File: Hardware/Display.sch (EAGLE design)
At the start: 54 parts, among them IC1 STM32F030C6T, IC2 VREG-TS1117CW-3V3, M1 WIRELESS-NRF24L01, Q1 BSS138, Q10 BSS138, Q11 IRLML5203, Q12 BSS138, Q13 IRLML5203, Q14 BSS138, Q15 IRLML5203, Q16 BSS138, Q2 BSS138, Q3 BSS138, Q4 BSS138, Q5 BSS138, Q6 BSS138, Q7 BSS138, Q8 BSS138, Q9 IRLML5203

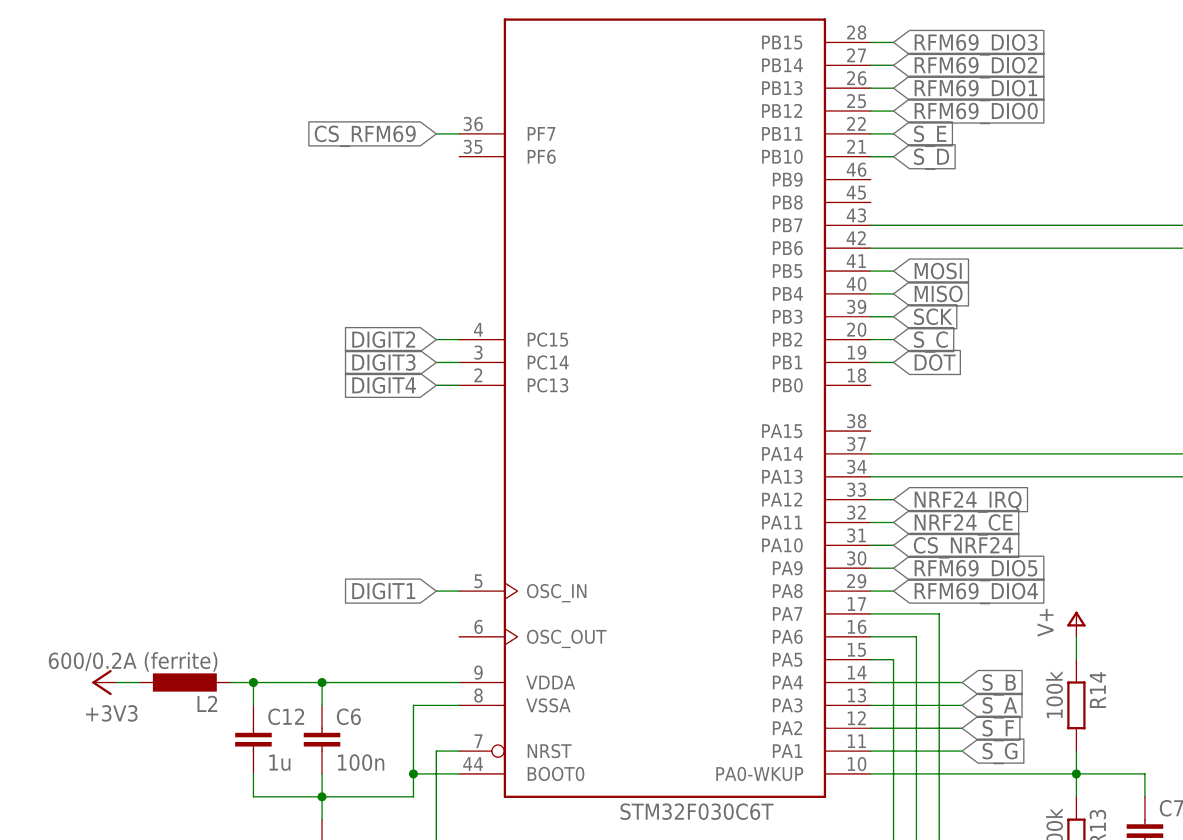
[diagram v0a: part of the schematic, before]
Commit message: Added crystal to display board
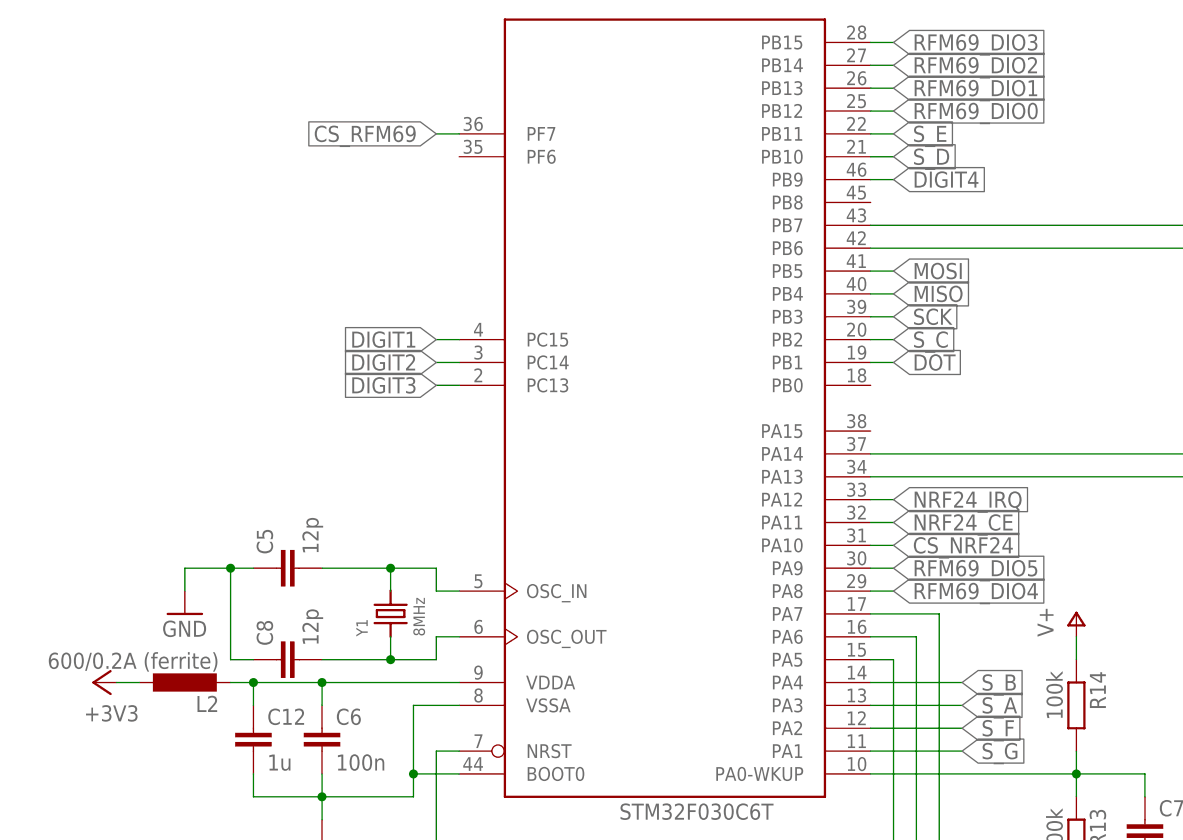
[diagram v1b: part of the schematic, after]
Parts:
- added C5, C8: 12p, rcl:C-EUC0603
- added Y1: 8MHz, abracon:CRYSTAL.3.2X2.5MM
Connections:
- new net N$15: C5.2, IC1MCU.OSC_IN, Y1.2
- new net N$19: C8.2, IC1MCU.OSC_OUT, Y1.1
- net DIGIT1: now also IC1MCU.PC15; no longer IC1MCU.OSC_IN
- net DIGIT2: now also IC1MCU.PC14; no longer IC1MCU.PC15
- net DIGIT3: now also IC1MCU.PC13; no longer IC1MCU.PC14
- net DIGIT4: now also IC1MCU.PB9; no longer IC1MCU.PC13
- net GND: now also C5.1, C8.1
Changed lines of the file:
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@@
 <part name="IN2" library="con-lstb" deviceset="MA07-1" device=""/>
 <part name="OUT2" library="con-lstb" deviceset="MA07-1" device=""/>
+<part name="Y1" library="abracon" deviceset="CRYSTAL" device=".3.2X2.5MM" value="8MHz"/>
+<part name="C5" library="rcl" deviceset="C-EU" device="C0603" value="12p"/>
+<part name="C8" library="rcl" deviceset="C-EU" device="C0603" value="12p"/>
+<part name="GND22" library="supply1" deviceset="GND" device=""/>
 </parts>
 <sheets>
@@
 <instance part="IN2" gate="1" x="533.4" y="5.08" rot="R90"/>
 <instance part="OUT2" gate="1" x="533.4" y="60.96" rot="MR270"/>
+<instance part="Y1" gate="G$1" x="127" y="-15.24" rot="R90"/>
+<instance part="C5" gate="G$1" x="114.3" y="-10.16" rot="R90"/>
+<instance part="C8" gate="G$1" x="114.3" y="-20.32" rot="R90"/>
+<instance part="GND22" gate="1" x="104.14" y="-15.24"/>
 </instances>
 <busses>
@@
 <wire x1="223.52" y1="25.4" x2="223.52" y2="15.24" width="0.1524" layer="91"/>
 </segment>
+<segment>
+<pinref part="GND22" gate="1" pin="GND"/>
+<wire x1="104.14" y1="-12.7" x2="104.14" y2="-10.16" width="0.1524" layer="91"/>
+<pinref part="C5" gate="G$1" pin="1"/>
+<wire x1="104.14" y1="-10.16" x2="109.22" y2="-10.16" width="0.1524" layer="91"/>
+<pinref part="C8" gate="G$1" pin="1"/>
+<wire x1="109.22" y1="-10.16" x2="111.76" y2="-10.16" width="0.1524" layer="91"/>
+<wire x1="111.76" y1="-20.32" x2="109.22" y2="-20.32" width="0.1524" layer="91"/>
+<wire x1="109.22" y1="-20.32" x2="109.22" y2="-10.16" width="0.1524" layer="91"/>
+<junction x="109.22" y="-10.16"/>
+</segment>
 </net>
 <net name="SCK" class="0">
@@
 </segment>
 <segment>
-<pinref part="IC1" gate="MCU" pin="OSC_IN"/>
-<wire x1="134.62" y1="-12.7" x2="132.08" y2="-12.7" width="0.1524" layer="91"/>
-<label x="132.08" y="-12.7" size="1.778" layer="95" rot="R180" xref="yes"/>
+<pinref part="IC1" gate="MCU" pin="PC15"/>
+<wire x1="134.62" y1="15.24" x2="132.08" y2="15.24" width="0.1524" layer="91"/>
+<label x="132.08" y="15.24" size="1.778" layer="95" rot="R180" xref="yes"/>
 </segment>
 </net>
@@
 </segment>
 <segment>
-<pinref part="IC1" gate="MCU" pin="PC15"/>
-<wire x1="134.62" y1="15.24" x2="132.08" y2="15.24" width="0.1524" layer="91"/>
-<label x="132.08" y="15.24" size="1.778" layer="95" rot="R180" xref="yes"/>
+<pinref part="IC1" gate="MCU" pin="PC14"/>
+<wire x1="134.62" y1="12.7" x2="132.08" y2="12.7" width="0.1524" layer="91"/>
+<label x="132.08" y="12.7" size="1.778" layer="95" rot="R180" xref="yes"/>
 </segment>
 </net>
@@
 </segment>
 <segment>
-<pinref part="IC1" gate="MCU" pin="PC14"/>
-<wire x1="134.62" y1="12.7" x2="132.08" y2="12.7" width="0.1524" layer="91"/>
-<label x="132.08" y="12.7" size="1.778" layer="95" rot="R180" xref="yes"/>
+<pinref part="IC1" gate="MCU" pin="PC13"/>
+<wire x1="134.62" y1="10.16" x2="132.08" y2="10.16" width="0.1524" layer="91"/>
+<label x="132.08" y="10.16" size="1.778" layer="95" rot="R180" xref="yes"/>
 </segment>
 </net>
@@
 </segment>
 <segment>
-<pinref part="IC1" gate="MCU" pin="PC13"/>
-<wire x1="134.62" y1="10.16" x2="132.08" y2="10.16" width="0.1524" layer="91"/>
-<label x="132.08" y="10.16" size="1.778" layer="95" rot="R180" xref="yes"/>
+<wire x1="180.34" y1="33.02" x2="182.88" y2="33.02" width="0.1524" layer="91"/>
+<label x="182.88" y="33.02" size="1.778" layer="95" xref="yes"/>
+<pinref part="IC1" gate="MCU" pin="PB9"/>
 </segment>
 </net>
@@
 </segment>
 </net>
+<net name="N$15" class="0">
+<segment>
+<pinref part="IC1" gate="MCU" pin="OSC_IN"/>
+<wire x1="134.62" y1="-12.7" x2="132.08" y2="-12.7" width="0.1524" layer="91"/>
+<wire x1="132.08" y1="-12.7" x2="132.08" y2="-10.16" width="0.1524" layer="91"/>
+<wire x1="132.08" y1="-10.16" x2="127" y2="-10.16" width="0.1524" layer="91"/>
+<pinref part="C5" gate="G$1" pin="2"/>
+<pinref part="Y1" gate="G$1" pin="2"/>
+<wire x1="127" y1="-10.16" x2="119.38" y2="-10.16" width="0.1524" layer="91"/>
+<wire x1="127" y1="-12.7" x2="127" y2="-10.16" width="0.1524" layer="91"/>
+<junction x="127" y="-10.16"/>
+</segment>
+</net>
+<net name="N$19" class="0">
+<segment>
+<pinref part="IC1" gate="MCU" pin="OSC_OUT"/>
+<wire x1="134.62" y1="-17.78" x2="132.08" y2="-17.78" width="0.1524" layer="91"/>
+<wire x1="132.08" y1="-17.78" x2="132.08" y2="-20.32" width="0.1524" layer="91"/>
+<wire x1="132.08" y1="-20.32" x2="127" y2="-20.32" width="0.1524" layer="91"/>
+<pinref part="C8" gate="G$1" pin="2"/>
+<pinref part="Y1" gate="G$1" pin="1"/>
+<wire x1="127" y1="-20.32" x2="119.38" y2="-20.32" width="0.1524" layer="91"/>
+<wire x1="127" y1="-17.78" x2="127" y2="-20.32" width="0.1524" layer="91"/>
+<junction x="127" y="-20.32"/>
+</segment>
+</net>
